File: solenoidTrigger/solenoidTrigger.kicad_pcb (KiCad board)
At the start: 2 copper layers, 88.9 x 88.9 mm, 51 parts, among them J1 Conn_01x05_Female, U2 ATmega328P-AU, Y2 Crystal_SMD

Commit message: starting adding fills
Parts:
- moved HFuseLED1 1.02 mm to (121.3, 119.4)
- moved R3 1.02 mm to (121.3, 114.7)
- turned sol_conn-3 to 180 degrees
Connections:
- fly-sol3 pad 1: /12V_Solenoid2 -> /12V_Solenoid3
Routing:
- net /CS: track 0.00 -> 57.3 mm, vias 0 -> 2
- net /ctrl_pin_3-1: track 0.00 -> 45.4 mm
- net /MOSI: track 25.4 -> 65.2 mm, vias 2 -> 4
- net /MISO: track 28.9 -> 65.7 mm, vias 0 -> 2
- net /12V_Switch: track 113.3 -> 149.9 mm
- net /ctrl_pin_3-2: track 0.00 -> 33.8 mm
- net /G0(IRQ): track 14.3 -> 45.9 mm
- net /12V_Solenoid3: track 0.00 -> 24.6 mm
- net /SCK: track 43.4 -> 54.1 mm
- net GND: track 37.5 -> 40.1 mm, vias 33 -> 41
- net /RESET: track 151.4 -> 153.3 mm
- net /ctrl_pin_2-2: track 47.8 -> 48.9 mm
- added copper zone on F.Cu, net (none)
- added copper zone on F.Cu, net /12V_Solenoid1

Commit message: finished unless i want to add a picture to the board
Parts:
- J1: value Conn_01x05_Female -> NoConnectRadio
- renumbered PowerLED1 to BLED1, fly-sol1 to FlySol1, fly-sol2 to FlySol2, fly-sol3 to FlySol3, HFuseLED1 to HFLED1, high_fuse1 to HFuse1, low_fuse1 to LFuse1, lin_reg1 to LinReg1, battery_conn1 to battery1, prog_conn1 to prog1, r_tres1_sol1 to r_tres1sol1, r_tres1_sol2 to r_tres1sol2, r_tres1_sol3 to r_tres1sol3, r_tres2_sol1 to r_tres2sol1, r_tres2_sol2 to r_tres2sol2, r_tres2_sol3 to r_tres2sol3, radio_conn1 to radio1, sol_conn-1 to sol1, sol_conn-2 to sol2, sol_conn-3 to sol3, tres1_sol1 to tres1sol1, tres1_sol2 to tres1sol2, tres1_sol3 to tres1sol3, tres2_sol1 to tres2sol1, tres2_sol2 to tres2sol2, tres2_sol3 to tres2sol3

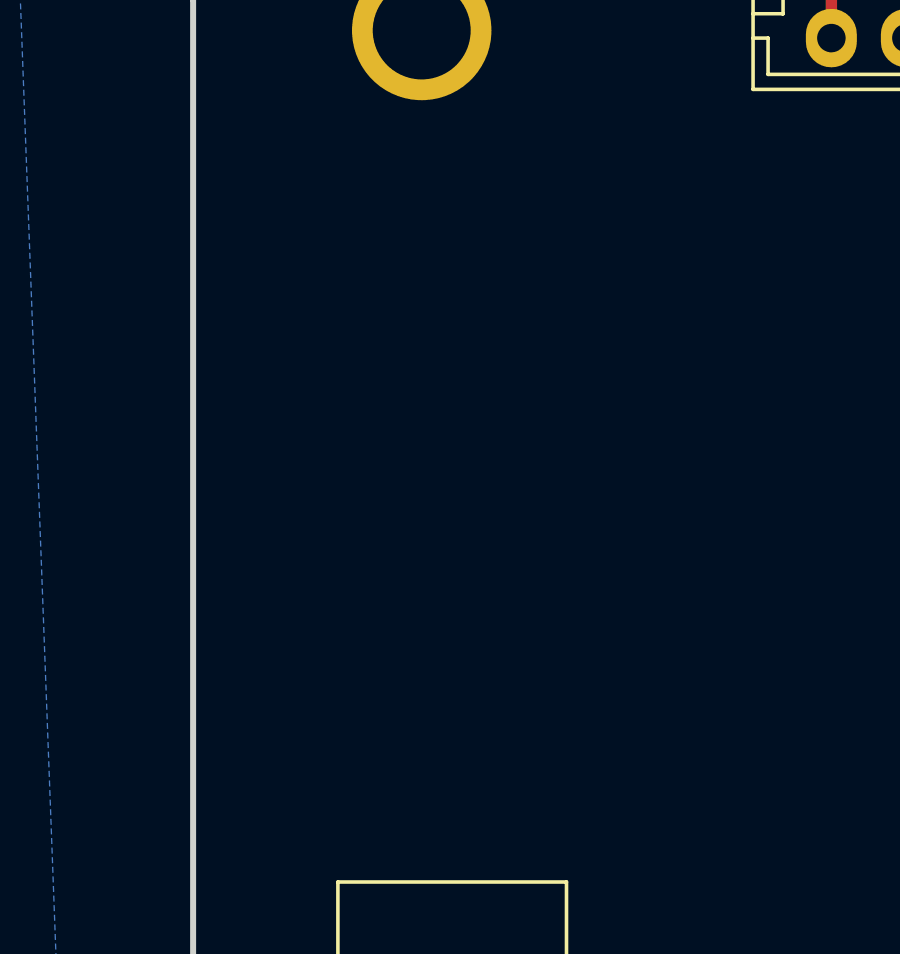
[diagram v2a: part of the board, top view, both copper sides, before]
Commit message: added name, data, and version number
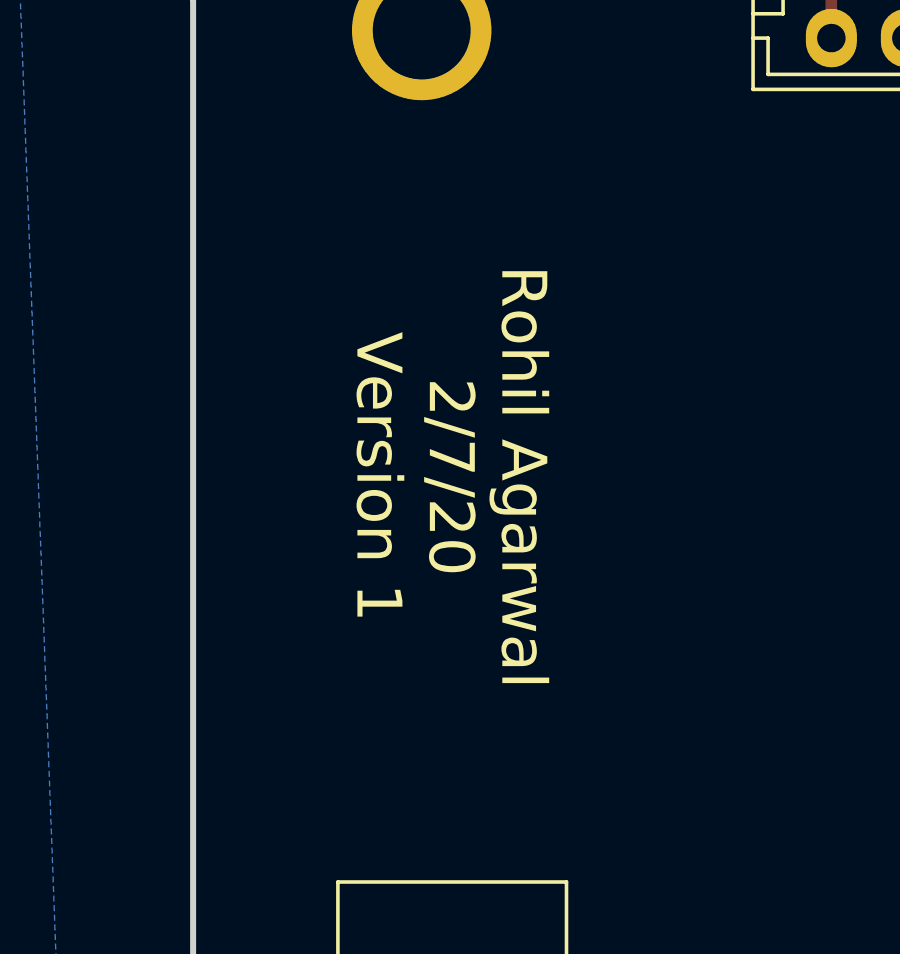
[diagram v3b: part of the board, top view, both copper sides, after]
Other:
- board text added: "Rohil Agarwal 2/7/20 Version 1"
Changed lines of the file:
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@@
   (general
     (thickness 1.6)
-    (drawings 8)
+    (drawings 9)
     (tracks 429)
     (zones 0)
@@
       (rotate (xyz 0 0 0))
     )
+  )
+  (gr_text "Rohil Agarwal\n2/7/20\nVersion 1" (at 111.4552 71.7804 270) (layer F.SilkS)
+    (effects (font (size 1.5 1.5) (thickness 0.3)))
   )
   (gr_line (start 191.77 132.08) (end 191.77 55.88) (layer Edge.Cuts) (width 0.2))
@@
   (segment (start 114.996 126.894) (end 119.293 131.191) (width 0.635) (layer F.Cu) (net 23))
   (segment (start 114.996 123.952) (end 114.996 126.894) (width 0.635) (layer F.Cu) (net 23))
-  (segment (start 121.3485 116.235) (end 121.3485 118.28) (width 0.254) (layer F.Cu) (net 47))
-  (segment (start 121.3485 115.631) (end 121.3485 116.235) (width 0.254) (layer F.Cu) (net 47))
   (segment (start 177.038 94.676) (end 177.038 99.103) (width 0.254) (layer F.Cu) (net 33))
   (segment (start 179.959 99.103998) (end 179.975501 99.120499) (width 0.254) (layer F.Cu) (net 34))
   (segment (start 179.959 94.676) (end 179.959 99.103998) (width 0.254) (layer F.Cu) (net 34))
   (segment (start 182.88 94.676) (end 182.88 99.103) (width 0.254) (layer F.Cu) (net 35))
-  (segment (start 113.096 123.952) (end 110.6375 123.952) (width 0.254) (layer F.Cu) (net 46))
   (segment (start 151.13 97.96) (end 151.13 95.565) (width 0.254) (layer F.Cu) (net 36))
   (segment (start 175.768 123.3805) (end 173.416 123.3805) (width 0.635) (layer F.Cu) (net 42))
@@
   (segment (start 176.8602 113.157) (end 175.768 113.157) (width 0.635) (layer F.Cu) (net 44))
   (segment (start 177.419 113.7158) (end 176.8602 113.157) (width 0.635) (layer F.Cu) (net 44))
+  (segment (start 113.096 123.952) (end 110.6375 123.952) (width 0.254) (layer F.Cu) (net 46))
+  (segment (start 121.3485 116.235) (end 121.3485 118.28) (width 0.254) (layer F.Cu) (net 47))
+  (segment (start 121.3485 115.631) (end 121.3485 116.235) (width 0.254) (layer F.Cu) (net 47))
   (zone (net 1) (net_name GND) (layer B.Cu) (hatch edge 0.508)
     (connect_pads (clearance 0.508))

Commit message: DONE WITH TEST BOARD
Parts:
- added G***: , footprints:OLIN_O, F.Cu at (135.3, 94.3)
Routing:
- net /SCK: track 54.1 -> 41.3 mm
- net GND: track 40.1 -> 43.3 mm, vias 41 -> 46
- net Net-(C6-Pad1): track 7.23 -> 8.52 mm
